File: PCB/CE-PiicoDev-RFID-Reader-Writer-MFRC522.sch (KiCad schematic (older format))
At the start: 49 parts, among them J1 , J2 , J3 Conn_PiicoDev_header_01x04_Ma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, J4 Conn_01x01_Male, J5 Conn_01x01_Male, U1 MFRC522, Y1 27.12MHz 12pF

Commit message: Update all
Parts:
- removed C?: 100n, symbol Device:C
- removed C?: 100p, symbol Device:C
- removed L3: L, symbol Device:L
- removed L?: 22nH, symbol Device:L
- added NT1, NT2, NT3, NT4, NT5: Net-Tie_2, PiicoDev RFID MFRC522:NetTie-2_SMD_Pad0.25mm, symbol Device:Net-Tie_2
- C1, C11, C12, C13, C3, C4: footprint (none) -> Capacitor_SMD:C_0402_1005Metric
- C10, C9: value C -> NP0 2%; footprint (none) -> Capacitor_SMD:C_0603_1608Metric
- C2, C7, C8: footprint (none) -> Capacitor_SMD:C_0603_1608Metric
- C5, C6: value 136p NP0 2% -> 120p NP0 2%; footprint (none) -> Capacitor_SMD:C_0603_1608Metric
- D2: footprint (none) -> CoreElectronics_Components:LED_1206_3216Metric_ReverseMount_Hole1.8x2.4mm
- J4: footprint (none) -> Connector_PinHeader_1.27mm:PinHeader_1x01_P1.27mm_Vertical
- J5: footprint (none) -> CoreElectronics_Components:PiicoDev_header_1pin_INT_uninverted
- JP3: footprint (none) -> CoreElectronics_Components:SolderJumper-2_P1.3mm_Bridged_RoundedPad1.0x1.5mm
- L1, L2: footprint (none) -> Inductor_SMD:L_0402_1005Metric
- R4, R5, R6, R7: footprint (none) -> Resistor_SMD:R_0603_1608Metric
- R8: footprint (none) -> Resistor_SMD:R_0402_1005Metric
- U1: footprint (none) -> Package_DFN_QFN:VQFN-32-1EP_5x5mm_P0.5mm_EP3.1x3.1mm
- Y1: footprint (none) -> Crystal:Crystal_SMD_3225-4Pin_3.2x2.5mm
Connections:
- net labels added: TURN1, TURN2, TURN3, TURN4, TURN5, TURN6
- wire segments 141 -> 139
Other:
- moved on the sheet: C1, C10, C11, C12, C13, C2, C3, C4, C5, C6, C7, C8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

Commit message: Update
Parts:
- removed Y1: 27.12MHz 12pF, Crystal:Crystal_SMD_3225-4Pin_3.2x2.5mm, symbol Device:Crystal
- added C14: 100n, Capacitor_SMD:C_0402_1005Metric, symbol Device:C
- added R9: 4k7, Resistor_SMD:R_0402_1005Metric, symbol Device:R
- added Y1: 27.12MHz 12pF, Crystal:Crystal_SMD_TXC_7M-4Pin_3.2x2.5mm, symbol Device:Crystal_GND24
- FID1, FID2: footprint Fiducial:Fiducial_1mm_Mask2mm -> CoreElectronics_Components:Fiducial_1mm_Mask2mm_No_Courtyard
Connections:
- wire segments 139 -> 154
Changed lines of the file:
@@
 F 0 "FID2" H 6785 7546 50  0001 L CNN
 F 1 "Fiducial" H 6785 7455 50  0001 L CNN
-F 2 "Fiducial:Fiducial_1mm_Mask2mm" H 6700 7500 50  0001 C CNN
+F 2 "CoreElectronics_Components:Fiducial_1mm_Mask2mm_No_Courtyard" H 6700 7500 50  0001 C CNN
 F 3 "~" H 6700 7500 50  0001 C CNN
 	1    6700 7500
@@
 F 0 "FID1" H 6785 7396 50  0001 L CNN
 F 1 "Fiducial" H 6785 7305 50  0001 L CNN
-F 2 "Fiducial:Fiducial_1mm_Mask2mm" H 6700 7350 50  0001 C CNN
+F 2 "CoreElectronics_Components:Fiducial_1mm_Mask2mm_No_Courtyard" H 6700 7350 50  0001 C CNN
 F 3 "~" H 6700 7350 50  0001 C CNN
 	1    6700 7350
@@
 Wire Wire Line
 	6050 3050 6450 3050
-Wire Wire Line
-	6250 3300 6450 3300
 Text Label 6250 3300 0    50   ~ 0
 RST
@@
 $EndComp
 Wire Wire Line
-	4900 2250 4900 2350
+	4900 2250 4900 2300
 Wire Wire Line
 	4900 2650 4900 2850
@@
 $EndComp
 $Comp
-L Device:C C13
-U 1 1 613BE34A
-P 5700 4600
-F 0 "C13" H 5815 4646 50  0000 L CNN
-F 1 "100n" H 5815 4555 50  0000 L CNN
-F 2 "Capacitor_SMD:C_0402_1005Metric" H 5738 4450 50  0001 C CNN
-F 3 "~" H 5700 4600 50  0001 C CNN
-	1    5700 4600
-	1    0    0    -1
-$EndComp
-$Comp
 L Device:C C12
 U 1 1 613BEE83
@@
 $EndComp
 Wire Wire Line
-	5700 4450 5700 4400
-Wire Wire Line
 	5700 4400 5350 4400
 Wire Wire Line
@@
 Wire Wire Line
 	5350 4800 5700 4800
-Text Notes 4600 4350 0    50   ~ 0
+Text Notes 4600 4150 0    50   ~ 0
 3 de-coupling caps should do the trick.\nNo reason for chosing 3 at this stage.
 Wire Wire Line
@@
 	7700 4450 8200 4450
 Wire Wire Line
-	7700 5000 9100 5000
-Wire Wire Line
 	8200 4450 8200 4750
 Wire Wire Line
 	8200 4750 8350 4750
-$Comp
-L Device:Crystal Y1
-U 1 1 614A7B4C
-P 8350 4550
-F 0 "Y1" V 8304 4681 50  0000 L CNN
-F 1 "27.12MHz 12pF" V 8395 4681 50  0000 L CNN
-F 2 "Crystal:Crystal_SMD_3225-4Pin_3.2x2.5mm" H 8350 4550 50  0001 C CNN
-F 3 "~" H 8350 4550 50  0001 C CNN
-	1    8350 4550
-	0    1    1    0
-$EndComp
 Wire Wire Line
 	7550 4350 8350 4350
@@
 Wire Wire Line
 	10750 3700 10750 4000
+$Comp
+L power:+3V3 #PWR0115
+U 1 1 613CB708
+P 5000 4350
+F 0 "#PWR0115" H 5000 4200 50  0001 C CNN
+F 1 "+3V3" H 5015 4523 50  0000 C CNN
+F 2 "" H 5000 4350 50  0001 C CNN
+F 3 "" H 5000 4350 50  0001 C CNN
+	1    5000 4350
+	1    0    0    -1
+$EndComp
+Wire Wire Line
+	5000 4350 5000 4400
+Connection ~ 5000 4400
+Wire Wire Line
+	5700 4450 5700 4400
+$Comp
+L Device:C C13
+U 1 1 613BE34A
+P 5700 4600
+F 0 "C13" H 5815 4646 50  0000 L CNN
+F 1 "100n" H 5815 4555 50  0000 L CNN
+F 2 "Capacitor_SMD:C_0402_1005Metric" H 5738 4450 50  0001 C CNN
+F 3 "~" H 5700 4600 50  0001 C CNN
+	1    5700 4600
+	1    0    0    -1
+$EndComp
+$Comp
+L Device:C C14
+U 1 1 613D9BBC
+P 6100 4600
+F 0 "C14" H 6215 4646 50  0000 L CNN
+F 1 "100n" H 6215 4555 50  0000 L CNN
+F 2 "Capacitor_SMD:C_0402_1005Metric" H 6138 4450 50  0001 C CNN
+F 3 "~" H 6100 4600 50  0001 C CNN
+	1    6100 4600
+	1    0    0    -1
+$EndComp
+Wire Wire Line
+	5700 4400 6100 4400
+Wire Wire Line
+	6100 4400 6100 4450
+Connection ~ 5700 4400
+Wire Wire Line
+	6100 4750 6100 4800
+Wire Wire Line
+	6100 4800 5700 4800
+$Comp
+L Device:R R9
+U 1 1 6140FFA0
+P 5550 3000
+F 0 "R9" H 5620 3046 50  0000 L CNN
+F 1 "4k7" H 5620 2955 50  0000 L CNN
+F 2 "Resistor_SMD:R_0402_1005Metric" V 5480 3000 50  0001 C CNN
+F 3 "~" H 5550 3000 50  0001 C CNN
+	1    5550 3000
+	1    0    0    -1
+$EndComp
+Wire Wire Line
+	4900 2300 5550 2300
+Wire Wire Line
+	5550 2300 5550 2850
+Connection ~ 4900 2300
+Wire Wire Line
+	4900 2300 4900 2350
+Wire Wire Line
+	5550 3150 5550 3300
+Wire Wire Line
+	5550 3300 6450 3300
+$Comp
+L Device:Crystal_GND24 Y1
+U 1 1 61423C54
+P 8350 4550
+F 0 "Y1" V 8304 4794 50  0000 L CNN
+F 1 "27.12MHz 12pF" V 8395 4794 50  0000 L CNN
+F 2 "Crystal:Crystal_SMD_TXC_7M-4Pin_3.2x2.5mm" H 8350 4550 50  0001 C CNN
+F 3 "~" H 8350 4550 50  0001 C CNN
+	1    8350 4550
+	0    1    1    0
+$EndComp
+Wire Wire Line
+	8550 4550 8600 4550
+Wire Wire Line
+	8600 4550 8600 5000
+Wire Wire Line
+	7700 5000 8100 5000
+Connection ~ 8600 5000
+Wire Wire Line
+	8600 5000 9100 5000
+Wire Wire Line
+	8150 4550 8100 4550
+Wire Wire Line
+	8100 4550 8100 5000
+Connection ~ 8100 5000
+Wire Wire Line
+	8100 5000 8600 5000
 $EndSCHEMATC

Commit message: Update
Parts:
- added 4k7: R, symbol Device:R
- added G4: Label_PCB_Art, PiicoDev RFID MFRC522:Label_Reset_Bar_Reverse Arrow, symbol CoreElectronics_Artwork:Label_PCB_Art
- added G5: Label_PCB_Art, PiicoDev RFID MFRC522:Label_Reset_Bar, symbol CoreElectronics_Artwork:Label_PCB_Art
- added NT10, NT11: Net-Tie_2, PiicoDev RFID MFRC522:NetTie-2_SMD_Pad0.25mm, symbol Device:Net-Tie_2
- added NT6, NT7, NT8, NT9: Net-Tie_2_Top, PiicoDev RFID MFRC522:NetTie-2_SMD_Pad0.25mm, symbol Device:Net-Tie_2
- added Q1: BSS138, Package_TO_SOT_SMD:SOT-23, symbol Transistor_FET:BSS138
- J4: footprint Connector_PinHeader_1.27mm:PinHeader_1x01_P1.27mm_Vertical -> Connector_PinHeader_2.54mm:PinHeader_1x01_P2.54mm_Vertical
- NT5: value Net-Tie_2 -> Net-Tie_2_Top
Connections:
- net GND: now also Q1.2 (S)
- net INT: now also Q1.1 (G); no longer D2.1 (K)
- net at D2.2 (A), R8.2: now also 4k7.1
- net RST renamed ~RST
- net TURN1 renamed TURN1A
- net TURN1A: now also NT5.1; no longer NT1.1
- net TURN2 renamed TURN2A
- net TURN2A: now also NT6.1; no longer NT2.1
- net TURN3 renamed TURN3A
- net TURN3A: now also NT7.1; no longer NT3.1
- net TURN4 renamed TURN4A
- net TURN4A: now also NT8.1; no longer NT4.1
- net TURN5 renamed TURN5A
- net TURN5A: now also NT9.1; no longer NT5.1
- net TURN6 renamed TURN1B
- net TURN1B: now also NT1.1; no longer R7.1
- new net: 4k7.2, D2.1 (K), Q1.3 (D)
- new net TURN2B: NT2.1, NT6.2
- new net TURN3B: NT3.1, NT7.2
- new net TURN4B: NT4.1, NT8.2
- new net TURN5B: NT10.1, NT9.2
- new net TURN6A: NT10.2, NT11.1
- new net TURN6B: NT11.2, R7.1
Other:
- note added: "~RST"
- note removed: "3 de-coupling caps should do the trick.\nNo reason for chosing 3 at this stage."
- note removed: "De-coupling caps\nConsider allowing for address change\nHeaders requird: Interrupt and RST\nJumper to change the address"
- moved on the sheet: NT1, NT2, NT3, NT4

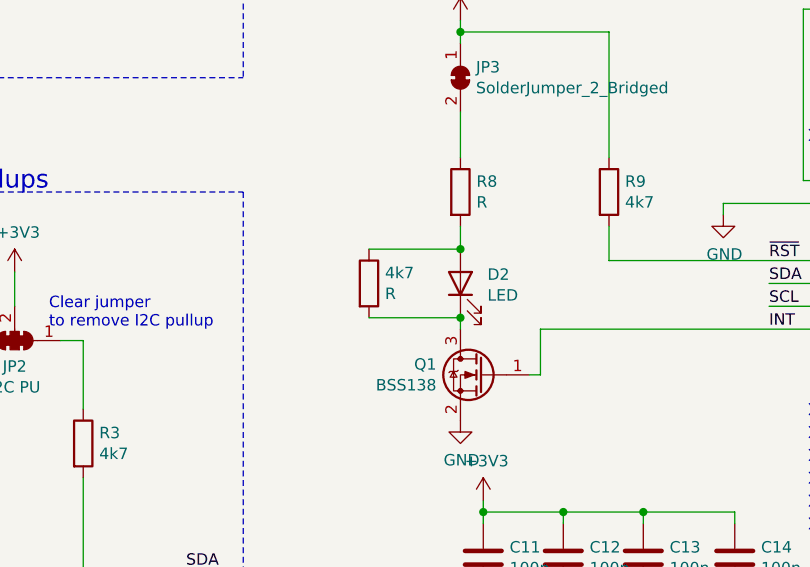
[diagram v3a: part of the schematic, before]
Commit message: Add R10
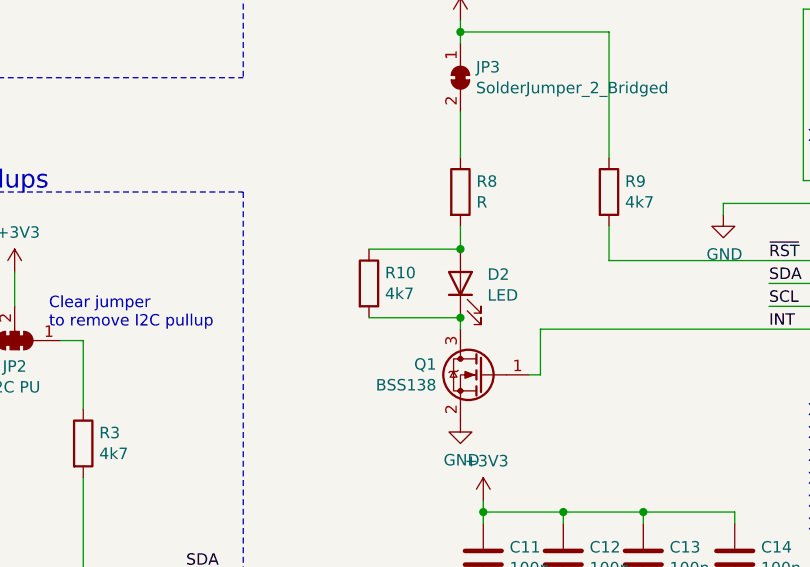
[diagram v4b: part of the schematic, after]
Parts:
- R10: renamed from 4k7; value R -> 4k7; footprint (none) -> Resistor_SMD:R_0402_1005Metric
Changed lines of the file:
@@
 $EndComp
 $Comp
-L Device:R 4k7
+L Device:R R10
 U 1 1 6175452D
 P 4500 3400
-F 0 "4k7" H 4570 3446 50  0000 L CNN
-F 1 "R" H 4570 3355 50  0000 L CNN
-F 2 "" V 4430 3400 50  0001 C CNN
+F 0 "R10" H 4570 3446 50  0000 L CNN
+F 1 "4k7" H 4570 3355 50  0000 L CNN
+F 2 "Resistor_SMD:R_0402_1005Metric" V 4430 3400 50  0001 C CNN
 F 3 "~" H 4500 3400 50  0001 C CNN
 	1    4500 3400

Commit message: Update CE-PiicoDev-RFID-Reader-Writer-MFRC522.sch
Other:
- note added: "Frequency\n13.56 MHz"
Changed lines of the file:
@@
 Text Notes 4100 6350 0    50   ~ 0
 ~RST
+Text Notes 6800 1400 0    50   ~ 0
+Frequency\n13.56 MHz
 $EndSCHEMATC

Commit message: Update
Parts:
- R8: value R -> 4k7
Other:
- note added: "Coil\nL = 2.7 uH\nR = 1.0 ohm\nQ = 230"
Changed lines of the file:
@@
 P 4900 3000
 F 0 "R8" H 4970 3046 50  0000 L CNN
-F 1 "R" H 4970 2955 50  0000 L CNN
+F 1 "4k7" H 4970 2955 50  0000 L CNN
 F 2 "Resistor_SMD:R_0402_1005Metric" V 4830 3000 50  0001 C CNN
 F 3 "~" H 4900 3000 50  0001 C CNN
@@
 Text Notes 6800 1400 0    50   ~ 0
 Frequency\n13.56 MHz
+Text Notes 12500 4500 0    50   ~ 0
+Coil\nL = 2.7 uH\nR = 1.0 ohm\nQ = 230
 $EndSCHEMATC

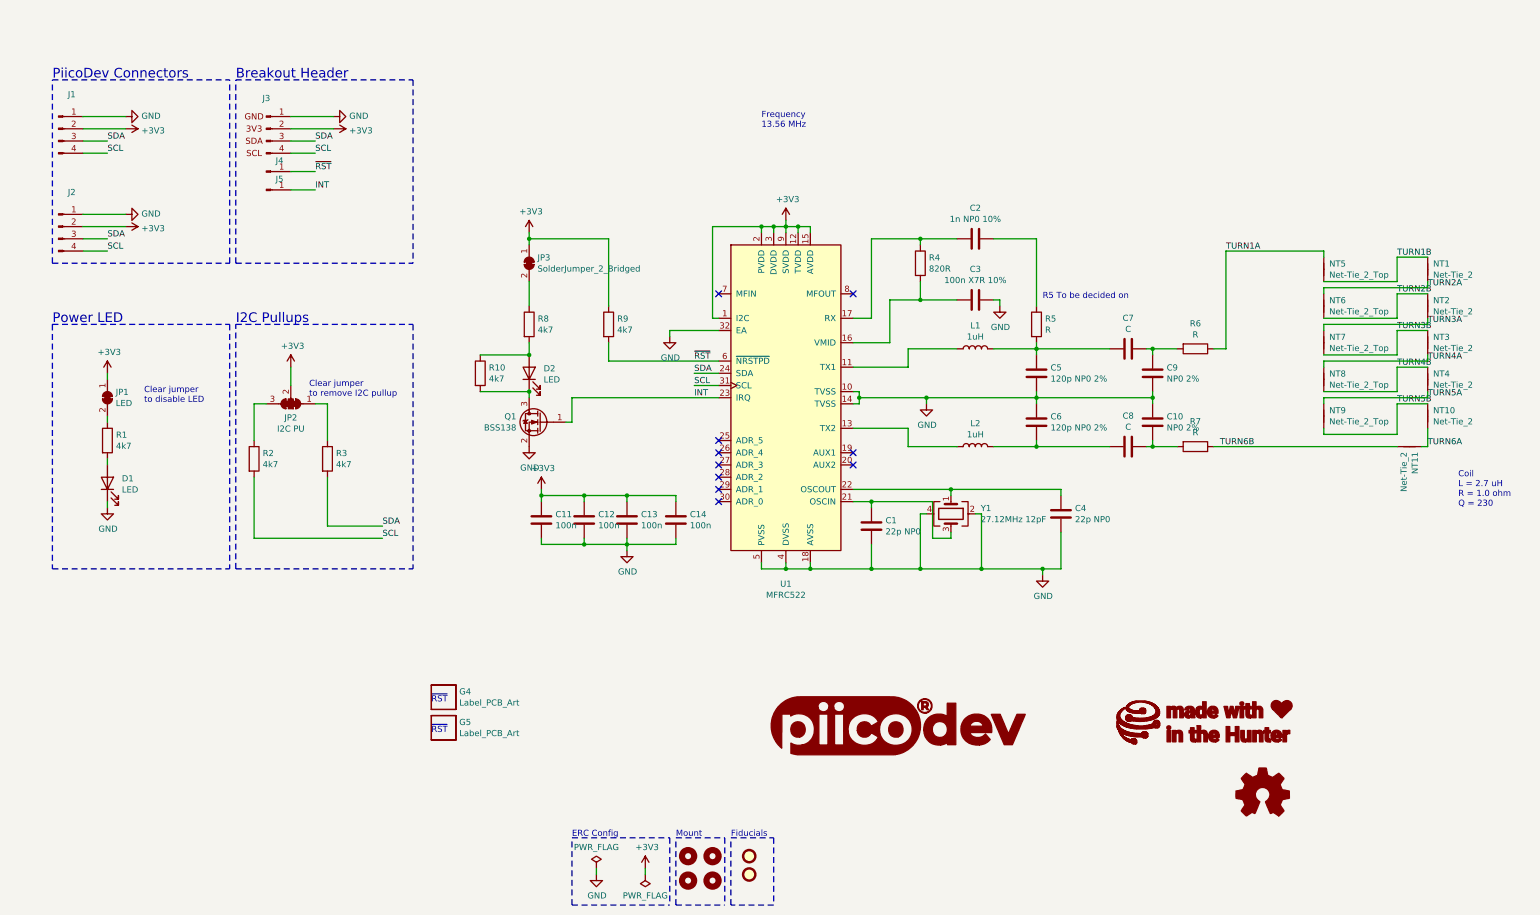
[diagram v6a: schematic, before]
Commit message: Change v00 to v01
Halve the coil length.
Make wider coil tracks.
Add test points.
Add I2C series resistor.
Change inductors from 0402 to 0603.
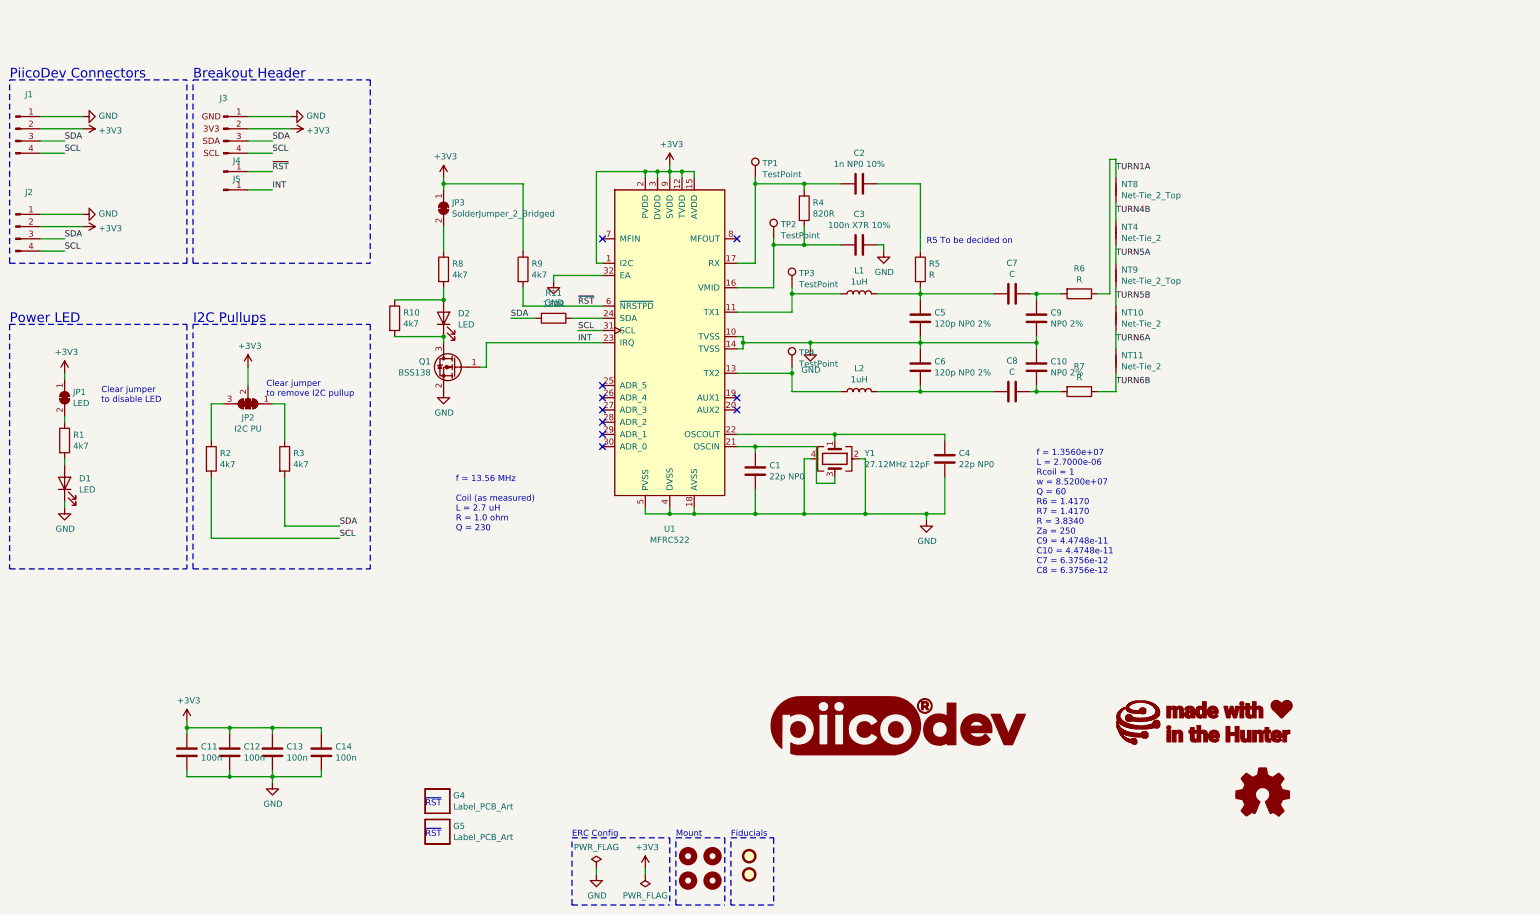
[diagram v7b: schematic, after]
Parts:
- removed NT1, NT2, NT3: Net-Tie_2, PiicoDev RFID MFRC522:NetTie-2_SMD_Pad0.25mm, symbol Device:Net-Tie_2
- removed NT5, NT6, NT7: Net-Tie_2_Top, PiicoDev RFID MFRC522:NetTie-2_SMD_Pad0.25mm, symbol Device:Net-Tie_2
- added R11: 120R, Resistor_SMD:R_0402_1005Metric, symbol Device:R
- added TP1, TP2, TP3, TP4: TestPoint, CoreElectronics_Components:TestPoint_Pad_0.7x0.7mm, symbol Connector:TestPoint
- J4: footprint Connector_PinHeader_2.54mm:PinHeader_1x01_P2.54mm_Vertical -> CoreElectronics_Components:PiicoDev_header_1pin
- L1, L2: footprint Inductor_SMD:L_0402_1005Metric -> Inductor_SMD:L_0603_1608Metric
- NT10, NT11, NT4, NT8, NT9: footprint PiicoDev RFID MFRC522:NetTie-2_SMD_Pad0.25mm -> PiicoDev RFID MFRC522:NetTie-2_SMD_Pad0.80mm
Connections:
- net TURN4A is gone; now on net TURN1A: NT8.1
- net SDA: now also R11.2; no longer U1.24 (SDA)
- net at C2.2, R4.1, U1.17 (RX): now also TP1.1
- net at C3.2, R4.2, U1.16 (VMID): now also TP2.1
- net at L1.1, U1.11 (TX1): now also TP3.1
- net at L2.1, U1.13 (TX2): now also TP4.1
- new net: R11.1, U1.24 (SDA)
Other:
- note added: "f = 1.3560e+07\nL = 2.7000e-06\nRcoil = 1\nw = 8.5200e+07\nQ = 60\nR6 = 1.4170\nR7 = 1.4170\nR = 3.8340\nZa = 250\nC9 = 4.4748e-11\nC10 = 4.4748e-11\nC7 = 6.3756e-12\nC8 = 6.3756e-12"
- note added: "f = 13.56 MHz\n\nCoil (as measured)\nL = 2.7 uH\nR = 1.0 ohm\nQ = 230"
- note removed: "Coil\nL = 2.7 uH\nR = 1.0 ohm\nQ = 230"
- note removed: "Frequency\n13.56 MHz"
- moved on the sheet: C1, C10, C11, C12, C13, C14, C2, C3, C4, C5, C6, C7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

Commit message: Update
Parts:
- removed R7: R, Resistor_SMD:R_0603_1608Metric, symbol Device:R
- added C15, C16: 270p NP0 2%, Capacitor_SMD:C_0603_1608Metric, symbol Device:C
- added JP4: SolderJumper_2_Open, CoreElectronics_Components:SolderJumper-2_P1.3mm_Open_RoundedPad1.0x1.5mm, symbol Jumper:SolderJumper_2_Open
- C10, C9: value NP0 2% -> 270p NP0 2%
- C5, C6: value 120p NP0 2% -> 62p NP0 2%
- C7, C8: value C -> 56p
- R1, R2, R3, R9: value 4k7 -> 10k
- R5: value R -> 470R
- R6: value R -> 10k; footprint Resistor_SMD:R_0603_1608Metric -> Resistor_SMD:R_0402_1005Metric
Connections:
- net +3V3: now also U1.28 (ADR_2), JP4.1 (A)
- net GND: now also R6.2, U1.25 (ADR_5), U1.26 (ADR_4), U1.27 (ADR_3), U1.29 (ADR_1), C15.2, C16.1
- net TURN1A: now also C7.1, C9.1, C15.1; no longer R6.1
- net TURN6B: now also C10.2, C8.1, C16.2
- net at U1.30 (ADR_0): now also R6.1, JP4.2 (B)
- no-connect marks 10 -> 4
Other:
- note added: "/Design Files/MFRC522.m"
- note added: "f = 13.56 MHz\n\nCoil (as measured)\nL = 470 nH\nR = 0.3 ohm"
- note removed: "f = 1.3560e+07\nL = 2.7000e-06\nRcoil = 1\nw = 8.5200e+07\nQ = 60\nR6 = 1.4170\nR7 = 1.4170\nR = 3.8340\nZa = 250\nC9 = 4.4748e-11\nC10 = 4.4748e-11\nC7 = 6.3756e-12\nC8 = 6.3756e-12"
- note removed: "f = 13.56 MHz\n\nCoil (as measured)\nL = 2.7 uH\nR = 1.0 ohm\nQ = 230"
- moved on the sheet: NT10, NT11, NT4, NT8, NT9
